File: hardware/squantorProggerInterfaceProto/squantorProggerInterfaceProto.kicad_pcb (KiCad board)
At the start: 2 copper layers, 2 parts

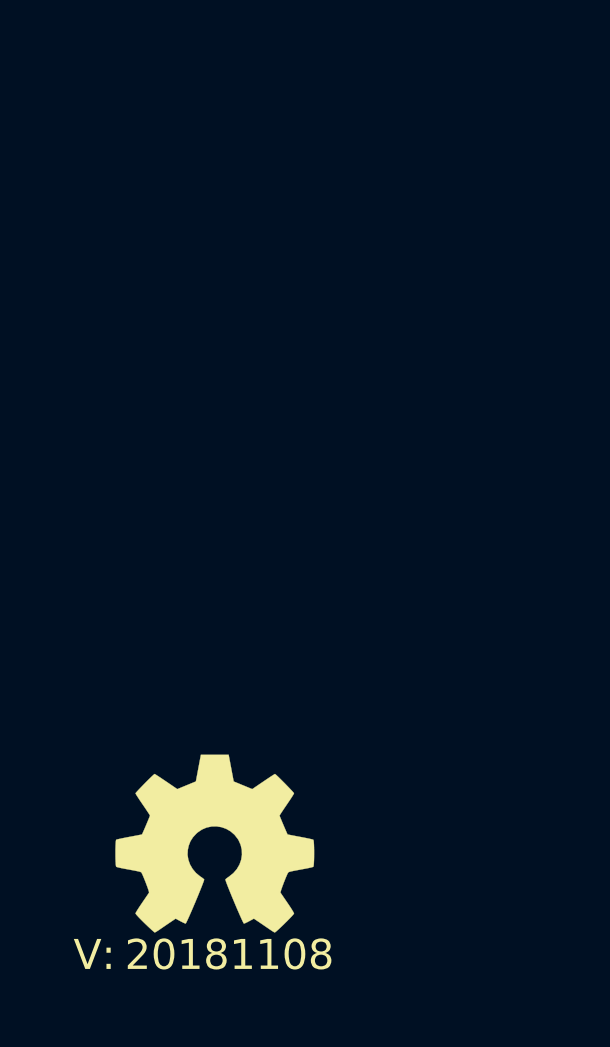
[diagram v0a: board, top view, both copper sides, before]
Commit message: initial placement of components
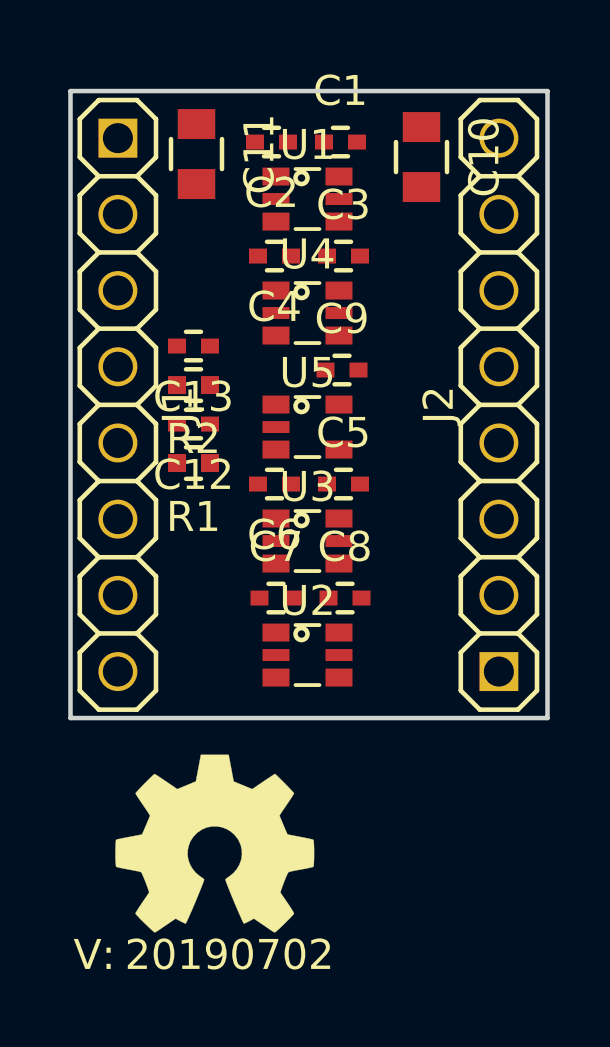
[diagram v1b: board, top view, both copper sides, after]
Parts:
- added C1: 100n, SquantorRcl:C_0402, F.Cu at (152.2, 77.6)
- added C10: 2.2uF, SquantorRcl:C_0805, F.Cu at (154.9, 78.1)
- added C11: 2.2uF, SquantorRcl:C_0805, F.Cu at (147.4, 78.0)
- added C12: 22p, SquantorRcl:C_0402, F.Cu at (147.3, 87.0)
- added C13: 22p, SquantorRcl:C_0402, F.Cu at (147.3, 84.4)
- added C2: 100n, SquantorRcl:C_0402, F.Cu at (149.9, 77.6)
- added C3: 100n, SquantorRcl:C_0402, F.Cu at (152.3, 81.4)
- added C4: 100n, SquantorRcl:C_0402, F.Cu at (150.0, 81.4)
- added C5: 100n, SquantorRcl:C_0402, F.Cu at (152.3, 89.0)
- added C6: 100n, SquantorRcl:C_0402, F.Cu at (150.0, 89.0)
- added C7: 100n, SquantorRcl:C_0402, F.Cu at (150.1, 92.8)
- added C8: 100n, SquantorRcl:C_0402, F.Cu at (152.3, 92.8)
- added C9: 100n, SquantorRcl:C_0402, F.Cu at (152.2, 85.2)
- added J1: JTAG_interface_proto_input, SquantorConnectors:Header-0254-1X08-H010, F.Cu at (144.8, 86.4)
- added J2: JTAG_interface_proto_output, SquantorConnectors:Header-0254-1X08-H010, F.Cu at (157.5, 86.4)
- added R1: TBD, SquantorRcl:R_0402_hand, F.Cu at (147.3, 88.3)
- added R2: TBD, SquantorRcl:R_0402_hand, F.Cu at (147.3, 85.7)
- added U1: 74X1T45, SquantorIC:SOT363-hand, F.Cu at (151.1, 79.5)
- added U2: 74X1T45, SquantorIC:SOT363-hand, F.Cu at (151.1, 94.7)
- added U3: 74X1T45, SquantorIC:SOT363-hand, F.Cu at (151.1, 90.9)
- added U4: 74X1T45, SquantorIC:SOT363-hand, F.Cu at (151.1, 83.3)
- added U5: 74X1G125, SquantorIC:SOT353-hand, F.Cu at (151.1, 87.1)
- N2: value 20181108 -> 20190702
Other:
- board outline added: 15.9 x 20.9 mm

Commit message: added named connectors to schematic, moved silk
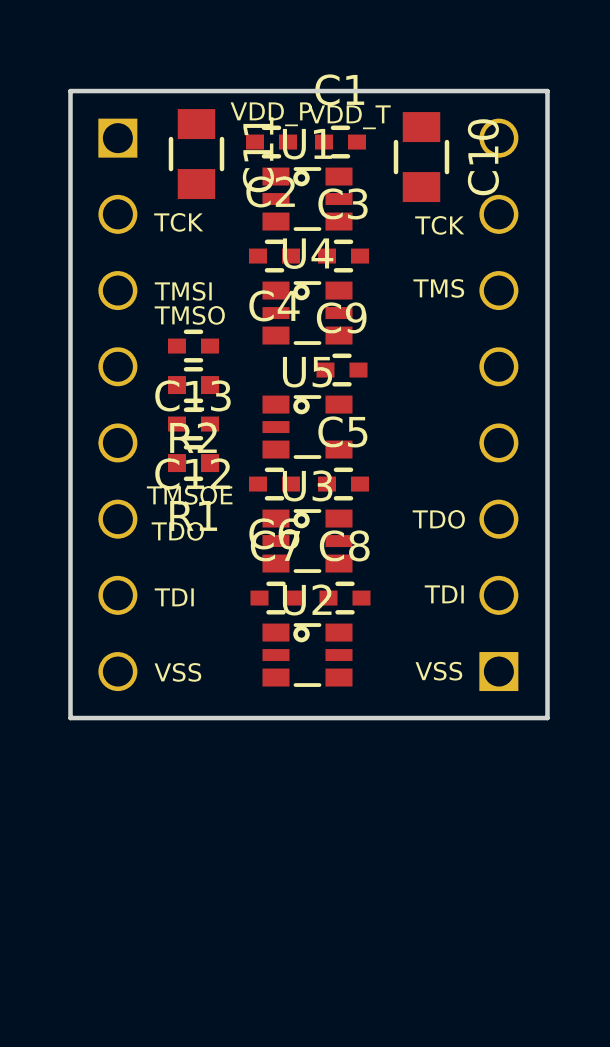
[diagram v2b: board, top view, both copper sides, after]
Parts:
- J1: footprint SquantorConnectors:Header-0254-1X08-H010 -> SquantorConnectorsNamed:JTAG-interface-proto-input; moved to B.Cu
- J2: footprint SquantorConnectors:Header-0254-1X08-H010 -> SquantorConnectorsNamed:JTAG-interface-proto-output; moved to B.Cu
- N1: moved to B.Cu
- N2: value 20190702 -> 20190703; moved to B.Cu
- moved N1 9.33 mm to (150.8, 92.1), turned to 180 degrees
- moved N2 9.30 mm to (150.8, 95.7)

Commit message: routing completed, no DRC errors
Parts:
- moved C8 2.55 mm to (149.8, 92.8), turned to 180 degrees
- moved C7 2.45 mm to (152.5, 92.8)
- moved R1 1.30 mm to (147.3, 87.0)
- moved C12 1.25 mm to (147.3, 88.2)
- moved C1 0.20 mm to (152.4, 77.6)
- moved C2 0.20 mm to (149.7, 77.6)
- moved C3 0.20 mm to (152.5, 81.4)
- moved C4 0.20 mm to (149.8, 81.4)
- moved C5 0.20 mm to (152.5, 89.0)
- moved C6 0.20 mm to (149.8, 89.0)
- moved C9 0.15 mm to (152.4, 85.2)
- turned C10 to 90 degrees
- turned C11 to 90 degrees
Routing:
- net /VDD_PROG: track 0.00 -> 37.6 mm, vias 0 -> 4
- net /VDD_TARGET: track 0.00 -> 37.2 mm, vias 0 -> 5
- net /TMS_TARGET: track 0.00 -> 11.4 mm
- net Net-(C13-Pad1): track 0.00 -> 6.73 mm
- net /TDI_TARGET: track 0.00 -> 6.46 mm
- net /TDI_PROG: track 0.00 -> 6.40 mm
- net /TDO_TARGET: track 0.00 -> 5.94 mm
- net /TMSI_PROG: track 0.00 -> 5.89 mm
- net /TDO_PROG: track 0.00 -> 5.88 mm
- net /TCK_TARGET: track 0.00 -> 5.43 mm
- net /TCK_PROG: track 0.00 -> 5.37 mm
- net Net-(C12-Pad1): track 0.00 -> 3.74 mm
- net /TMSO_PROG: track 0.00 -> 3.49 mm
- net /TMSOE_PROG: track 0.00 -> 3.45 mm
- net /VSS: track 0.00 -> 2.79 mm, vias 0 -> 8
- added copper zone on B.Cu, net /VSS
- added copper zone on F.Cu, net /VSS
